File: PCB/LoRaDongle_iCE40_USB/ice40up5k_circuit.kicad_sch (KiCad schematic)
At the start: 38 parts, among them IC2 ICE40UP5K-UWG30ITR1K, IC3 SGP40-D-R4, J3 Conn_01x08_Male, J4 Conn_01x04_Male, J6 Conn_02x02_Top_Bottom, SW1 SW_Push, SW2 SW_Push, U5 W25Q128JVS, X1 ECS-2520MV-500-BL-TR

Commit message: updated routing
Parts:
- J6: Manufacturer (none) -> -; Manufacturer Part Number (none) -> -; Package (none) -> -
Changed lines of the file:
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@@
+      (effects (font (size 1.27 1.27)) hide)
+    )
+    (property "Description" "2x02 Male Header" (id 4) (at 36.068 32.258 0)
+      (effects (font (size 1.27 1.27)) hide)
+    )
+    (property "Manufacturer" "-" (id 5) (at 36.068 32.258 0)
+      (effects (font (size 1.27 1.27)) hide)
+    )
+    (property "Manufacturer Part Number" "-" (id 6) (at 36.068 32.258 0)
+      (effects (font (size 1.27 1.27)) hide)
+    )
+    (property "Package" "-" (id 7) (at 36.068 32.258 0)
       (effects (font (size 1.27 1.27)) hide)
     )

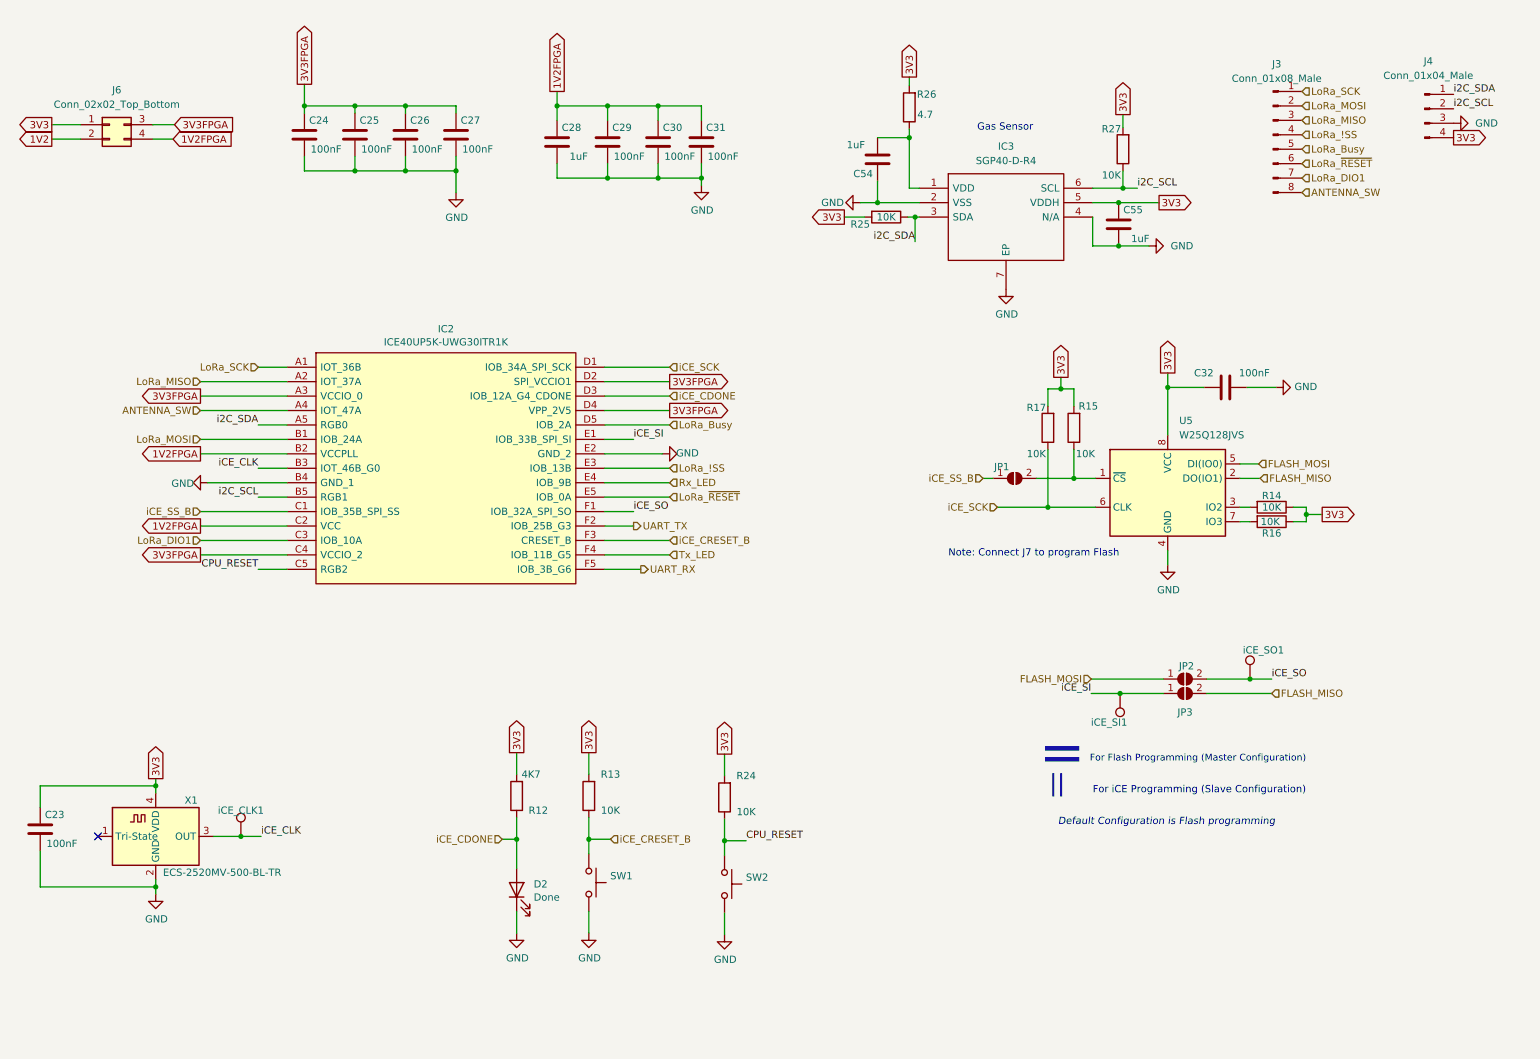
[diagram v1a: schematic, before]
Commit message: updated schematic to QFN ice40
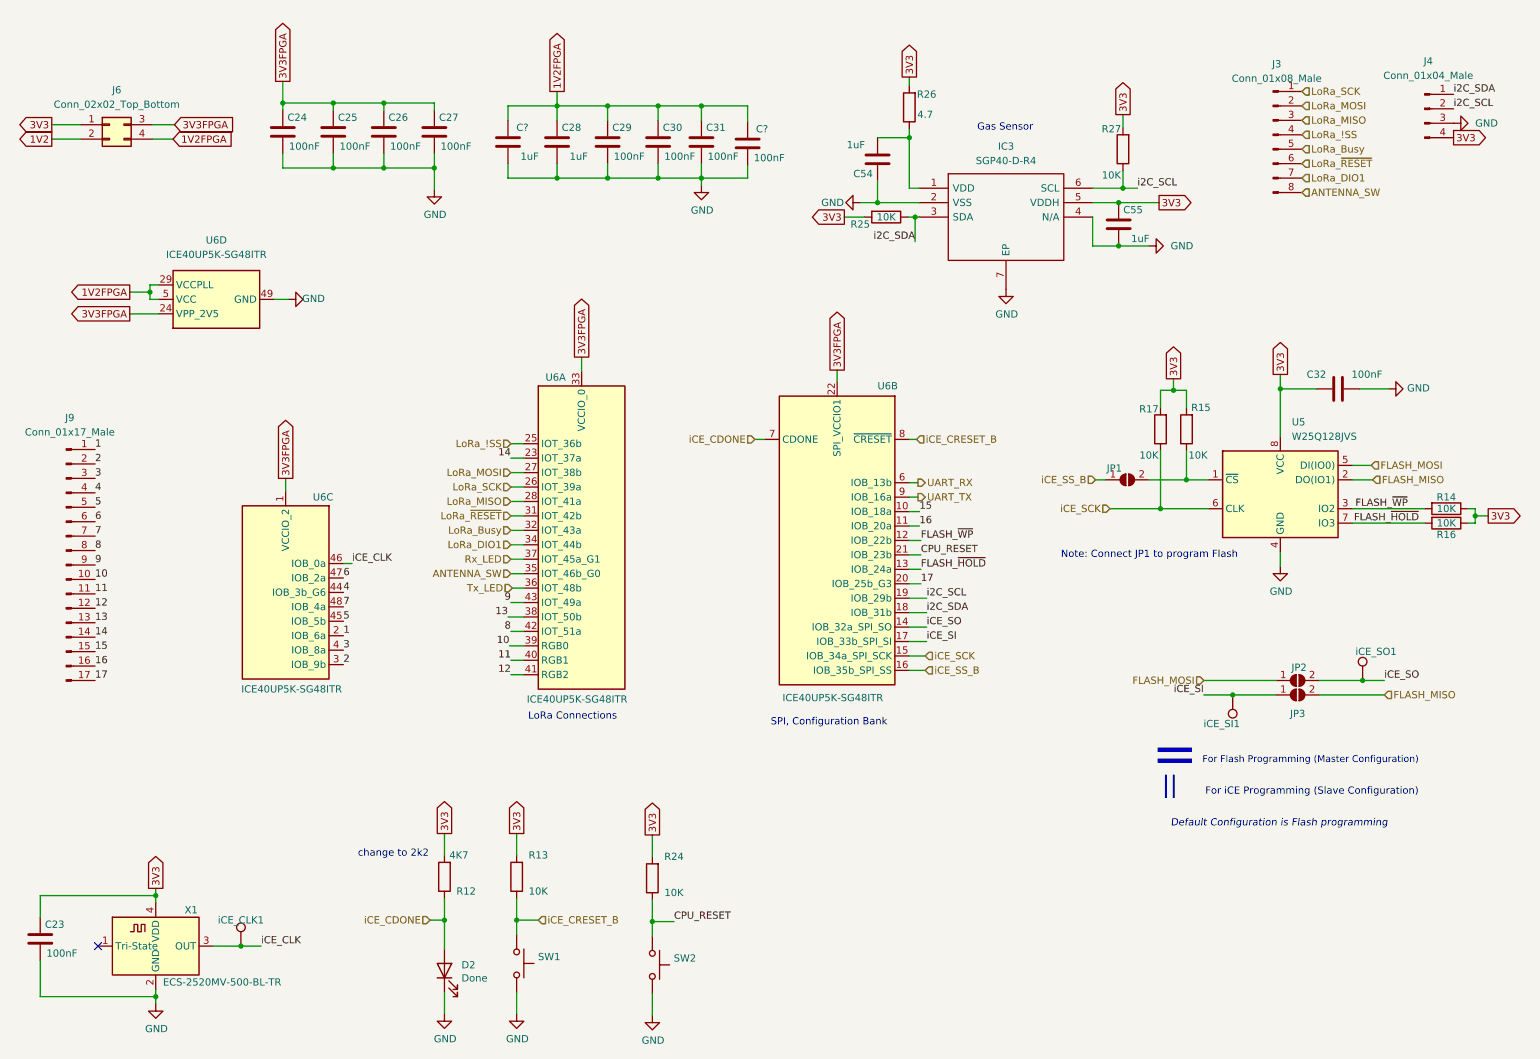
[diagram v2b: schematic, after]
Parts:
- removed IC2: ICE40UP5K-UWG30ITR1K, ICE40UP5K-UWG30ITR1K_KiCad:BGA30C40P5X6_211X254X60, symbol ICE40UP5K-UWG30ITR1K:ICE40UP5K-UWG30ITR1K
- added C?: 100nF, Capacitor_SMD:C_0402_1005Metric_Pad0.74x0.62mm_HandSolder, symbol Device:C
- added C?: 1uF, Capacitor_SMD:C_0402_1005Metric_Pad0.74x0.62mm_HandSolder, symbol Device:C
- added J9: Conn_01x17_Male, Connector_PinHeader_2.54mm:PinHeader_1x17_P2.54mm_Vertical, symbol Connector:Conn_01x17_Male
- added U6: ICE40UP5K-SG48ITR, Package_DFN_QFN:QFN-48-1EP_7x7mm_P0.5mm_EP5.6x5.6mm, symbol FPGA_Lattice:ICE40UP5K-SG48ITR
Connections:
- net 1V2FPGA: now also C?.2, C?.2, U6.29 (VCCPLL), U6.30 (VCC), U6.5 (VCC)
- net 3V3FPGA: now also U6.1 (VCCIO_2), U6.22 (SPI_VCCIO1), U6.24 (VPP_2V5), U6.33 (VCCIO_0)
- net ANTENNA_SW: now also U6.35 (IOT_46b_G0)
- net CPU_RESET: now also U6.21 (IOB_23b)
- net GND: now also C?.1, C?.1, U6.49 (GND)
- net LoRa_!SS: now also U6.25 (IOT_36b)
- net LoRa_Busy: now also U6.32 (IOT_43a)
- net LoRa_DIO1: now also U6.34 (IOT_44b)
- net LoRa_MISO: now also U6.28 (IOT_41a)
- net LoRa_MOSI: now also U6.27 (IOT_38b)
- net LoRa_SCK: now also U6.26 (IOT_39a)
- net LoRa_~{RESET}: now also U6.31 (IOT_42b)
- net Rx_LED: now also U6.37 (IOT_45a_G1)
- net Tx_LED: now also U6.36 (IOT_48b)
- net UART_RX: now also U6.6 (IOB_13b)
- net UART_TX: now also U6.9 (IOB_16a)
- net i2C_SCL: now also U6.19 (IOB_29b)
- net i2C_SDA: now also U6.18 (IOB_31b)
- net iCE_CDONE: now also U6.7 (CDONE)
- net iCE_CLK: now also U6.46 (IOB_0a)
- net iCE_CRESET_B: now also U6.8 (~{CRESET})
- net iCE_SCK: now also U6.15 (IOB_34a_SPI_SCK)
- net iCE_SI: now also U6.17 (IOB_33b_SPI_SI)
- net iCE_SO: now also U6.14 (IOB_32a_SPI_SO)
- net iCE_SS_B: now also U6.16 (IOB_35b_SPI_SS)
- net FLASH_~{HOLD}: now reaches R16.2, U5.7 (IO3)
- net FLASH_~{HOLD}: now also U6.13 (IOB_24a)
- net FLASH_~{WP}: now reaches R14.2, U5.3 (IO2)
- net FLASH_~{WP}: now also U6.12 (IOB_22b)
- new net 1: J9.1 (Pin_1), U6.2 (IOB_6a)
- new net 10: J9.10 (Pin_10), U6.39 (RGB0)
- new net 11: J9.11 (Pin_11), U6.40 (RGB1)
- new net 12: J9.12 (Pin_12), U6.41 (RGB2)
- new net 13: J9.13 (Pin_13), U6.38 (IOT_50b)
- new net 14: J9.14 (Pin_14), U6.23 (IOT_37a)
- new net 15: J9.15 (Pin_15), U6.10 (IOB_18a)
- new net 16: J9.16 (Pin_16), U6.11 (IOB_20a)
- new net 17: J9.17 (Pin_17), U6.20 (IOB_25b_G3)
- new net 2: J9.2 (Pin_2), U6.3 (IOB_9b)
- new net 3: J9.3 (Pin_3), U6.4 (IOB_8a)
- new net 4: J9.4 (Pin_4), U6.44 (IOB_3b_G6)
- new net 5: J9.5 (Pin_5), U6.45 (IOB_5b)
- new net 6: J9.6 (Pin_6), U6.47 (IOB_2a)
- new net 7: J9.7 (Pin_7), U6.48 (IOB_4a)
- new net 8: J9.8 (Pin_8), U6.42 (IOT_51a)
- new net 9: J9.9 (Pin_9), U6.43 (IOT_49a)
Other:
- note added: "LoRa Connections"
- note added: "Note: Connect JP1 to program Flash"
- note added: "SPI, Configuration Bank"
- note added: "change to 2k2"
- note removed: "Note: Connect J7 to program Flash"
- moved on the sheet: C23, C24, C25, C26, C27, C32, D2, JP1, JP2, JP3, R12, R13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

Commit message: updated routing
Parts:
- D2: Manufacturer Part Number XZVG53W-8 -> XZCBD53W-1
- R12: value 4K7 -> 2k2; Manufacturer Stackpole Electronics Inc -> Yageo; Manufacturer Part Number RMCF0402JT4K70 -> RC0402FR-072K2L
- gave numbers to parts that had none: 2
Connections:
- net 1 renamed Pin1
- net Pin1: now also U6.4 (IOB_8a); no longer U6.2 (IOB_6a)
- net 10 renamed Pin10
- net Pin10: now also U6.41 (RGB2); no longer U6.39 (RGB0)
- net 11 renamed Pin11
- net 12 renamed Pin12
- net Pin12: now also U6.39 (RGB0); no longer U6.41 (RGB2)
- net 13 renamed Pin13
- net 14 renamed Pin14
- net Pin14: now also U6.10 (IOB_18a); no longer U6.23 (IOT_37a)
- net 15 renamed Pin15
- net Pin15: now also U6.11 (IOB_20a); no longer U6.10 (IOB_18a)
- net 16 renamed Pin16
- net Pin16: now also U6.20 (IOB_25b_G3); no longer U6.11 (IOB_20a)
- net 17 renamed Pin17
- net Pin17: now also U6.23 (IOT_37a); no longer U6.20 (IOB_25b_G3)
- net 2 renamed Pin2
- net 3 renamed Pin3
- net Pin3: now also U6.2 (IOB_6a); no longer U6.4 (IOB_8a)
- net 4 renamed Pin4
- net Pin4: now also U6.48 (IOB_4a); no longer U6.44 (IOB_3b_G6)
- net 5 renamed Pin5
- net Pin5: now also U6.47 (IOB_2a); no longer U6.45 (IOB_5b)
- net 6 renamed Pin6
- net Pin6: now also U6.45 (IOB_5b); no longer U6.47 (IOB_2a)
- net 7 renamed Pin7
- net Pin7: now also U6.44 (IOB_3b_G6); no longer U6.48 (IOB_4a)
- net 8 renamed Pin8
- net Pin8: now also U6.43 (IOT_49a); no longer U6.42 (IOT_51a)
- net 9 renamed Pin9
- net Pin9: now also U6.42 (IOT_51a); no longer U6.43 (IOT_49a)
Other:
- note removed: "change to 2k2"

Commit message: routing complete
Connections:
- net ANTENNA_SW: now also J3.5 (Pin_5); no longer J3.8 (Pin_8)
- net LoRa_Busy: now also J3.7 (Pin_7); no longer J3.5 (Pin_5)
- net LoRa_DIO1: now also J3.8 (Pin_8); no longer J3.7 (Pin_7)
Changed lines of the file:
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@@
     (effects (font (size 1.27 1.27)) (justify right))
   )
-  (hierarchical_label "ANTENNA_SW" (shape input) (at 245.872 44.196 0)
+  (hierarchical_label "ANTENNA_SW" (shape input) (at 245.872 36.576 0)
     (effects (font (size 1.27 1.27)) (justify left))
   )
@@
     (effects (font (size 1.27 1.27)) (justify left))
   )
-  (hierarchical_label "LoRa_Busy" (shape input) (at 245.872 36.576 0)
+  (hierarchical_label "LoRa_Busy" (shape input) (at 245.872 41.656 0)
     (effects (font (size 1.27 1.27)) (justify left))
   )
@@
     (effects (font (size 1.27 1.27)) (justify left))
   )
-  (hierarchical_label "LoRa_DIO1" (shape input) (at 245.872 41.656 0)
+  (hierarchical_label "LoRa_DIO1" (shape input) (at 245.872 44.196 0)
     (effects (font (size 1.27 1.27)) (justify left))
   )

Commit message: updated BOM
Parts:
- IC3: Manufacturer (none) -> Sensirion AG; Manufacturer Part Number (none) -> SGP40-D-R4; Package (none) -> DFN
- J9: Manufacturer (none) -> -; Manufacturer Part Number (none) -> -; Package (none) -> -
- SW1, SW2: Package (none) -> Through Hole
- U6: Manufacturer (none) -> Lattice Semiconductor; Manufacturer Part Number (none) -> ICE40UP5K-SG48ITR50; Package (none) -> 48-QFN
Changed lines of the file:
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@@
+      (effects (font (size 1.27 1.27)) hide)
+    )
+    (property "Package" "Through Hole" (id 8) (at 107.696 179.832 0)
       (effects (font (size 1.27 1.27)) hide)
     )
@@
     )
     (property "Datasheet" "http://www.latticesemi.com/Products/FPGAandCPLD/iCE40Ultra" (id 3) (at 108.966 78.232 0)
+      (effects (font (size 1.27 1.27)) hide)
+    )
+    (property "Manufacturer" "Lattice Semiconductor" (id 4) (at 119.126 103.632 0)
+      (effects (font (size 1.27 1.27)) hide)
+    )
+    (property "Manufacturer Part Number" "ICE40UP5K-SG48ITR50" (id 5) (at 119.126 103.632 0)
+      (effects (font (size 1.27 1.27)) hide)
+    )
+    (property "Package" "48-QFN" (id 6) (at 119.126 103.632 0)
       (effects (font (size 1.27 1.27)) hide)
     )
@@
       (effects (font (size 1.27 1.27)) hide)
     )
+    (property "Package" "Through Hole" (id 8) (at 131.572 180.086 0)
+      (effects (font (size 1.27 1.27)) hide)
+    )
     (pin "1")
     (pin "2")
@@
     )
     (property "Datasheet" "http://www.latticesemi.com/Products/FPGAandCPLD/iCE40Ultra" (id 3) (at 174.244 80.01 0)
+      (effects (font (size 1.27 1.27)) hide)
+    )
+    (property "Manufacturer" "Lattice Semiconductor" (id 4) (at 164.084 105.41 0)
+      (effects (font (size 1.27 1.27)) hide)
+    )
+    (property "Manufacturer Part Number" "ICE40UP5K-SG48ITR50" (id 5) (at 164.084 105.41 0)
+      (effects (font (size 1.27 1.27)) hide)
+    )
+    (property "Package" "48-QFN" (id 6) (at 164.084 105.41 0)
       (effects (font (size 1.27 1.27)) hide)
     )
@@
       (effects (font (size 1.27 1.27)) hide)
     )
+    (property "Manufacturer" "Lattice Semiconductor" (id 4) (at 54.864 62.992 0)
+      (effects (font (size 1.27 1.27)) hide)
+    )
+    (property "Manufacturer Part Number" "ICE40UP5K-SG48ITR50" (id 5) (at 54.864 62.992 0)
+      (effects (font (size 1.27 1.27)) hide)
+    )
+    (property "Package" "48-QFN" (id 6) (at 54.864 62.992 0)
+      (effects (font (size 1.27 1.27)) hide)
+    )
     (pin "23")
     (pin "25")
@@
       (effects (font (size 1.27 1.27)) hide)
     )
+    (property "Description" "RES 0 OHM JUMPER 1/10W 0603" (id 8) (at 245.11 132.588 0)
+      (effects (font (size 1.27 1.27)) hide)
+    )
     (pin "1")
     (pin "2")
@@
     )
     (property "Type" "SMD" (id 7) (at 215.138 94.742 0)
+      (effects (font (size 1.27 1.27)) hide)
+    )
+    (property "Description" "RES 0 OHM JUMPER 1/10W 0603" (id 8) (at 215.138 94.742 0)
       (effects (font (size 1.27 1.27)) hide)
     )
@@
       (effects (font (size 1.27 1.27)) hide)
     )
+    (property "Description" "RES 0 OHM JUMPER 1/10W 0603" (id 8) (at 245.11 130.048 0)
+      (effects (font (size 1.27 1.27)) hide)
+    )
     (pin "1")
     (pin "2")
@@
     )
     (property "Datasheet" "http://www.latticesemi.com/Products/FPGAandCPLD/iCE40Ultra" (id 3) (at 77.216 89.154 0)
+      (effects (font (size 1.27 1.27)) hide)
+    )
+    (property "Manufacturer" "Lattice Semiconductor" (id 4) (at 67.056 114.554 0)
+      (effects (font (size 1.27 1.27)) hide)
+    )
+    (property "Manufacturer Part Number" "ICE40UP5K-SG48ITR50" (id 5) (at 67.056 114.554 0)
+      (effects (font (size 1.27 1.27)) hide)
+    )
+    (property "Package" "48-QFN" (id 6) (at 67.056 114.554 0)
       (effects (font (size 1.27 1.27)) hide)
     )
@@
       (effects (font (size 1.27 1.27)) hide)
     )
+    (property "Description" "1x17 Male Header" (id 4) (at 28.448 109.728 0)
+      (effects (font (size 1.27 1.27)) hide)
+    )
+    (property "Manufacturer" "-" (id 5) (at 28.448 109.728 0)
+      (effects (font (size 1.27 1.27)) hide)
+    )
+    (property "Manufacturer Part Number" "-" (id 6) (at 28.448 109.728 0)
+      (effects (font (size 1.27 1.27)) hide)
+    )
+    (property "Package" "-" (id 7) (at 28.448 109.728 0)
+      (effects (font (size 1.27 1.27)) hide)
+    )
     (pin "1")
     (pin "10")
@@
       (effects (font (size 1.27 1.27)) (justify left) hide)
     )
-    (pin "1")
+    (property "Manufacturer" "Sensirion AG" (id 12) (at 178.562 43.434 0)
+      (effects (font (size 1.27 1.27)) hide)
+    )
+    (property "Manufacturer Part Number" "SGP40-D-R4" (id 13) (at 178.562 43.434 0)
+      (effects (font (size 1.27 1.27)) hide)
+    )
+    (property "Package" "DFN" (id 14) (at 178.562 43.434 0)
+      (effects (font (size 1.27 1.27)) hide)
+    )
+    (pin "1")
